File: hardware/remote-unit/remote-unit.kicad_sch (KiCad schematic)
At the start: 59 parts, among them J1 SOL_A, J2 RF Module, J3 ICSP, J5 SOL_B, J6 PWR 12V, J7 UART, J8 RS485, J9 SOLAR, Q1 N >1A@4VGS, Q2 PNP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

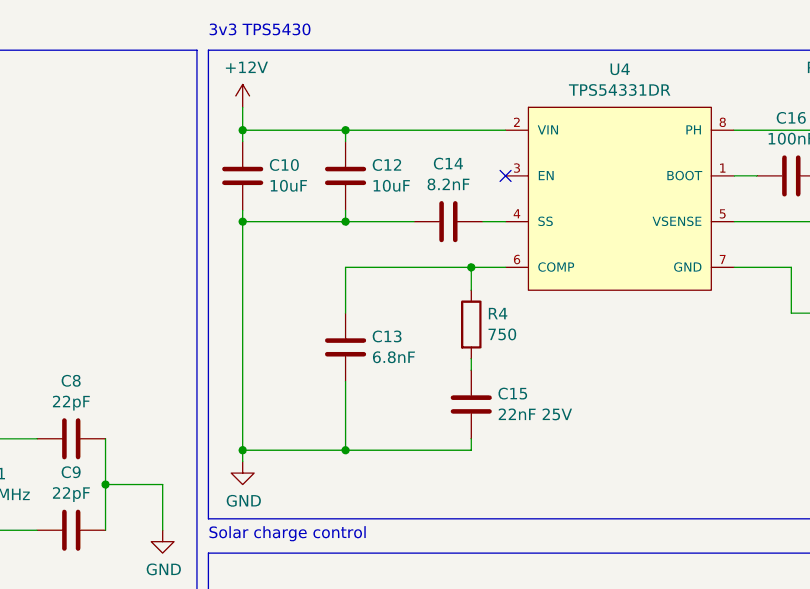
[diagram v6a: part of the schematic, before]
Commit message: Update remote unit buck converter
Update compensation network values.
Redo layout.
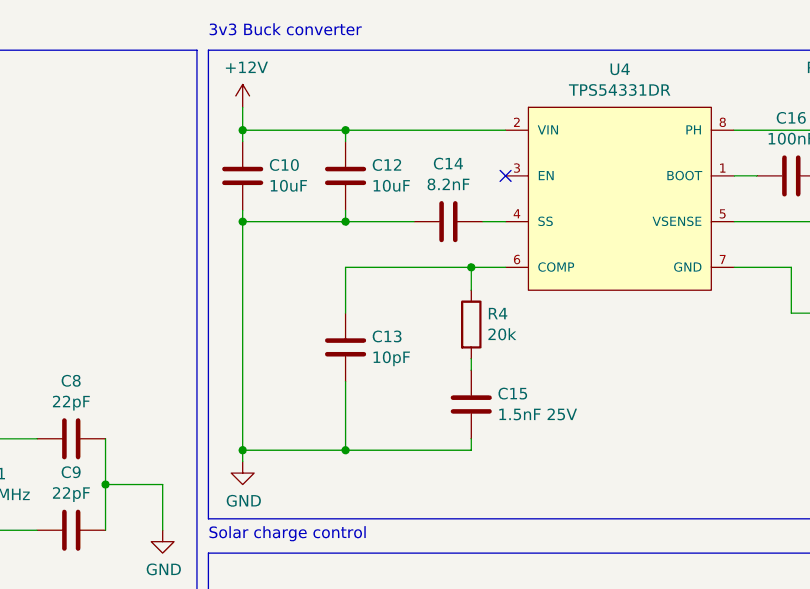
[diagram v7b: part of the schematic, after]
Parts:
- C13: value 6.8nF -> 10pF; JLCPCB Part C1631 -> C1634; Purchase Link NA -> (none)
- C15: value 22nF 25V -> 1.5nF 25V; JLCPCB Part C21122 -> C1595; Purchase Link NA -> (none)
- R4: value 750 -> 20k; footprint Resistor_SMD:R_0603_1608Metric -> Resistor_SMD:R_0402_1005Metric; JLCPCB Part C23241 -> C25765; Purchase Link NA -> (none)
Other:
- note added: "3v3 Buck converter"
- note removed: "3v3 TPS5430"
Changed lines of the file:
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@@
 	(title_block
 		(title "Irrigation Remote Unit")
-		(rev "1")
+		(rev "3")
 		(company "Daniel McMillan")
 	)
@@
 		)
 	)
-	(text "3v3 TPS5430"
+	(text "3v3 Buck converter"
 		(exclude_from_sim no)
 		(at 102.87 13.97 0)
@@
 			)
 		)
-		(property "Value" "750"
+		(property "Value" "20k"
 			(at 133.858 46.863 0)
 			(effects
@@
 			)
 		)
-		(property "Footprint" "Resistor_SMD:R_0603_1608Metric"
+		(property "Footprint" "Resistor_SMD:R_0402_1005Metric"
 			(at 130.302 45.72 90)
 			(effects
@@
 			)
 		)
-		(property "Datasheet" "https://datasheet.lcsc.com/lcsc/1811081723_UNI-ROYAL-Uniroyal-Elec-0603WAF7500T5E_C23241.pdf"
+		(property "Datasheet" "https://www.lcsc.com/datasheet/lcsc_datasheet_2206010100_UNI-ROYAL-Uniroyal-Elec-0402WGF2002TCE_C25765.pdf"
 			(at 132.08 45.72 0)
 			(effects
@@
 			)
 		)
-		(property "JLCPCB Part" "C23241"
-			(at 132.08 45.72 0)
-			(effects
-				(font
-					(size 1.27 1.27)
-				)
-				(hide yes)
-			)
-		)
-		(property "Purchase Link" "NA"
+		(property "JLCPCB Part" "C25765"
 			(at 132.08 45.72 0)
 			(effects
@@
 			)
 		)
-		(property "Value" "6.8nF"
+		(property "Value" "10pF"
 			(at 121.031 49.403 0)
 			(effects
@@
 			)
 		)
-		(property "Datasheet" "https://datasheet.lcsc.com/lcsc/1811061811_FH-Guangdong-Fenghua-Advanced-Tech-0603B682K500NT_C1631.pdf"
+		(property "Datasheet" "https://www.lcsc.com/datasheet/C1634.pdf"
 			(at 118.11 48.26 0)
 			(effects
@@
 			)
 		)
-		(property "JLCPCB Part" "C1631"
-			(at 118.11 48.26 0)
-			(effects
-				(font
-					(size 1.27 1.27)
-				)
-				(hide yes)
-			)
-		)
-		(property "Purchase Link" "NA"
+		(property "JLCPCB Part" "C1634"
 			(at 118.11 48.26 0)
 			(effects
@@
 			)
 		)
-		(property "Value" "22nF 25V"
+		(property "Value" "1.5nF 25V"
 			(at 135.001 55.753 0)
 			(effects
@@
 			)
 		)
-		(property "Datasheet" "https://datasheet.lcsc.com/lcsc/1811101610_Samsung-Electro-Mechanics-CL10B223KB8NNNC_C21122.pdf"
+		(property "Datasheet" "https://www.lcsc.com/datasheet/C1595.pdf"
 			(at 132.08 54.61 0)
 			(effects
@@
 			)
 		)
-		(property "JLCPCB Part" "C21122"
-			(at 132.08 54.61 0)
-			(effects
-				(font
-					(size 1.27 1.27)
-				)
-				(hide yes)
-			)
-		)
-		(property "Purchase Link" "NA"
+		(property "JLCPCB Part" "C1595"
 			(at 132.08 54.61 0)
 			(effects

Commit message: Update remote unit for jlcpcb fabrication
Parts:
- C1, F1, J8: now left out of the parts list
- C14: JLCPCB Part C1631 -> C1322360; Purchase Link NA (Note replaced with 6.8nF) -> (none)
- U2, U3: FT Rotation Offset (none) -> -90; Purchase Link NA (Extended) -> (none)
- U4: FT Rotation Offset (none) -> -90; Purchase Link NA -> (none)
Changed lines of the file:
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@@
 			)
 		)
-		(property "Purchase Link" "NA"
+		(property "FT Rotation Offset" "-90"
 			(at 133.35 24.13 0)
 			(effects
@@
 			)
 		)
-		(property "Datasheet" "https://datasheet.lcsc.com/lcsc/1811061811_FH-Guangdong-Fenghua-Advanced-Tech-0603B682K500NT_C1631.pdf"
+		(property "Datasheet" "https://wmsc.lcsc.com/wmsc/upload/file/pdf/v2/lcsc/2304140030_FH--Guangdong-Fenghua-Advanced-Tech-0603B822K500NT_C1322360.pdf"
 			(at 129.54 34.29 0)
 			(effects
@@
 			)
 		)
-		(property "JLCPCB Part" "C1631"
-			(at 129.54 34.29 0)
-			(effects
-				(font
-					(size 1.27 1.27)
-				)
-				(hide yes)
-			)
-		)
-		(property "Purchase Link" "NA (Note replaced with 6.8nF)"
+		(property "JLCPCB Part" "C1322360"
 			(at 129.54 34.29 0)
 			(effects
@@
 		(unit 1)
 		(exclude_from_sim no)
-		(in_bom yes)
+		(in_bom no)
 		(on_board yes)
 		(dnp no)
@@
 			)
 		)
-		(property "Purchase Link" "NA (Extended)"
+		(property "FT Rotation Offset" "-90"
 			(at 49.53 144.78 0)
 			(effects
@@
 		(unit 1)
 		(exclude_from_sim no)
-		(in_bom yes)
+		(in_bom no)
 		(on_board yes)
 		(dnp no)
@@
 			)
 		)
-		(property "Purchase Link" "NA (Extended)"
+		(property "FT Rotation Offset" "-90"
 			(at 49.53 177.8 0)
 			(effects
@@
 		(unit 1)
 		(exclude_from_sim no)
-		(in_bom yes)
+		(in_bom no)
 		(on_board yes)
 		(dnp no)
